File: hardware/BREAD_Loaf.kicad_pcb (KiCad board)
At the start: 2 copper layers, 35.4 x 50.7 mm, 33 parts, among them J2 THING_PLUS_LOGICAL, J6 PPPC101LGBN-RC, Q1 BSS138, Q2 BSS138, Q3 BSS138, U1 LTC4311ISC6-TRMPBF, U2 AP63205WU-7, U3 PCA9306

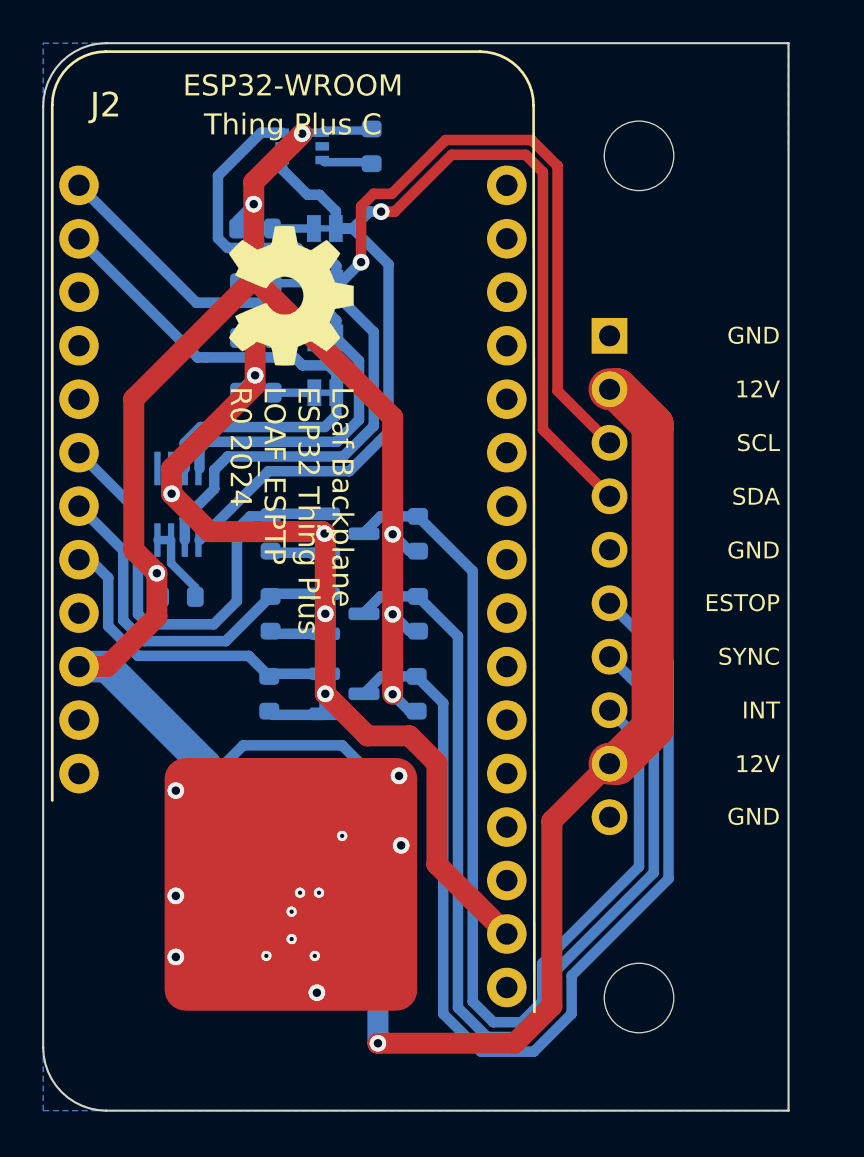
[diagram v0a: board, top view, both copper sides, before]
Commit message: added art and cleared erc errors
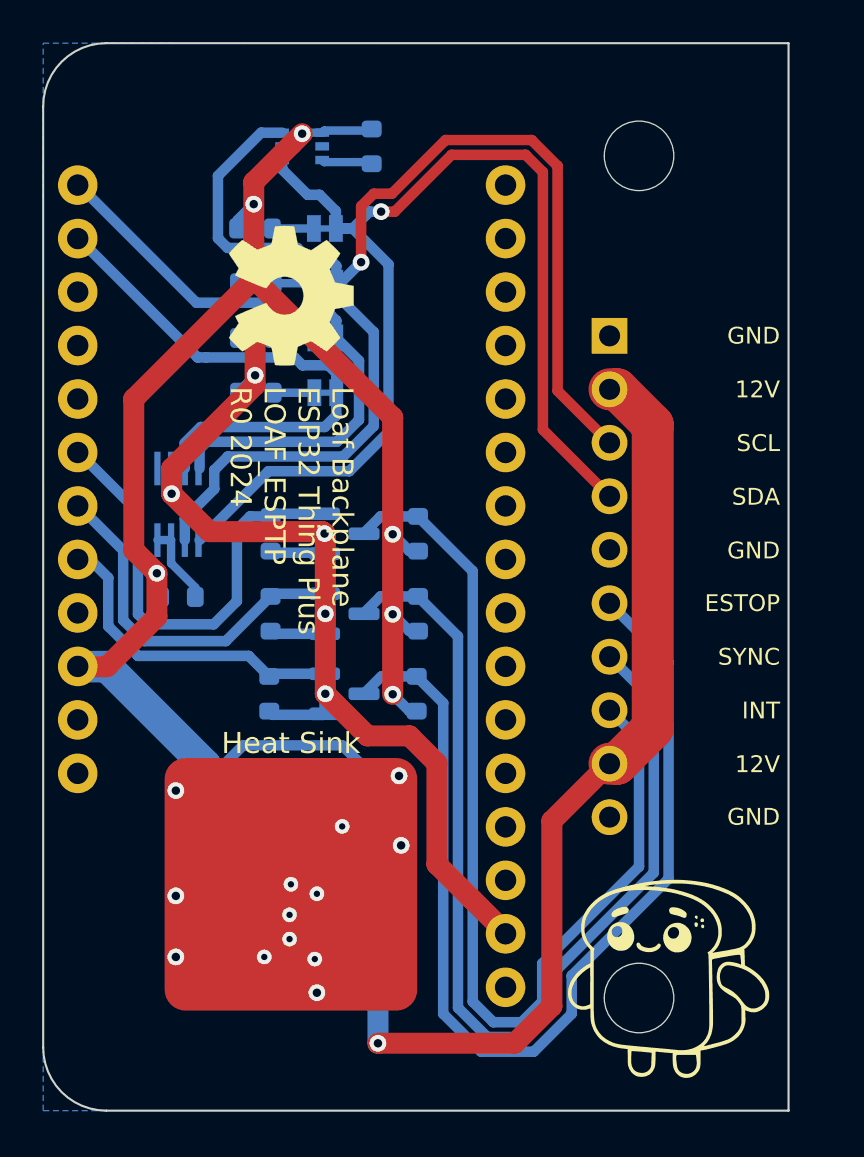
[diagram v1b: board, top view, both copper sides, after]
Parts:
- added demo**: Arc, Arc, F.Cu at (77.6, 122.4)
- added demo**: Arc, Arc, B.Cu at (86.4, 82.7)
- HS1: footprint SparkFun-Fuse:Thermal Pad -> KML-Custom:Thermal Pad
- J2: footprint SparkFun-RF:ESP_THING_PLUS -> SparkFun-Board:ThingPlus
- JP1, JP2, JP3, JP4: footprint SparkFun-Jumper:SMT-JUMPER_2_NC_TRACE_SILK -> SparkFun-Jumper:Jumper_2_NC_Trace
- ST1, ST2: footprint SparkFun-Hardware:STAND-OFF -> SparkFun-Hardware:Standoff
- moved J2 31.4 mm to (64.8, 102.6)

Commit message: updated to remove i2c shifter and optimized layout
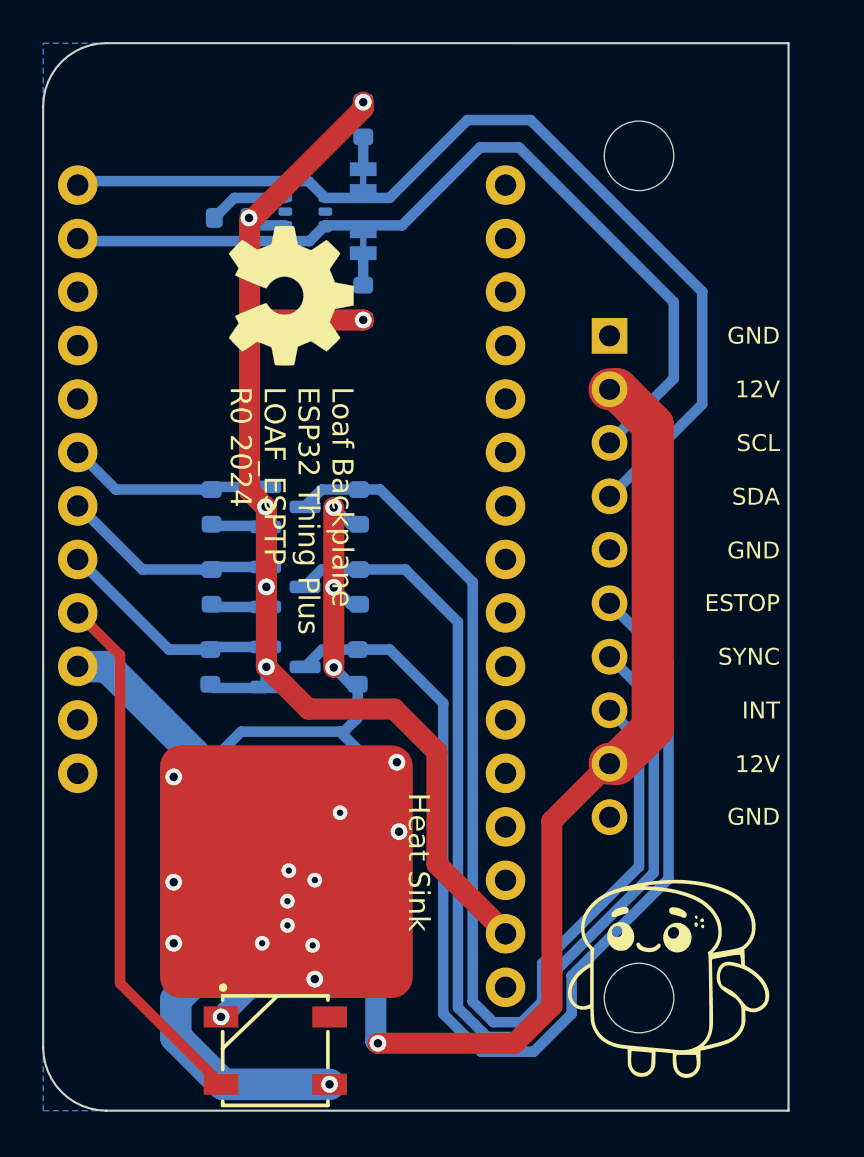
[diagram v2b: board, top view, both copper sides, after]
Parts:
- removed JP3, JP4: ~, SparkFun-Jumper:Jumper_2_NC_Trace
- removed R10, R12: 2.2k, Resistor_SMD:R_0603_1608Metric
- removed R11: 4.7k, Resistor_SMD:R_0603_1608Metric
- removed the U1 at (65.3, 77.9)
- removed U3: PCA9306, Package_SO:SSOP-8_2.95x2.8mm_P0.65mm
- removed the demo** at (86.4, 82.7)
- added D1: WS2812B_5050, SparkFun-LED:WS2812-5050-4PIN, F.Cu at (64.0, 120.8)
- added U2: LTC4311ISC6-TRMPBF, Package_TO_SOT_SMD:SOT-363_SC-70-6, B.Cu at (65.5, 81.0)
- R8: value 200k -> 2.2k
- R9: value 4.7k -> 2.2k
- moved R8 24.3 mm to (68.2, 76.6), turned to -90 degrees
- moved R7 7.47 mm to (62.0, 81.3), turned to 180 degrees
- moved R9 6.23 mm to (68.2, 85.3), turned to 90 degrees
- moved Q1 3.08 mm to (64.5, 102.6)
- moved R1 3.08 mm to (60.9, 102.6)
- moved R4 3.08 mm to (67.9, 102.6)
- moved Q2 3.08 mm to (64.5, 98.8)
- moved Q3 3.08 mm to (64.5, 95.0)
- moved R2 3.08 mm to (61.0, 98.8)
- moved R3 3.08 mm to (61.0, 95.0)
- moved R5 3.08 mm to (68.0, 98.8)
- moved R6 3.08 mm to (68.0, 95.0)
- moved JP1 2.93 mm to (68.2, 79.5), turned to -90 degrees
- moved JP2 2.65 mm to (68.2, 82.5), turned to 90 degrees
- moved C1 0.66 mm to (67.3, 114.3)
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- renumbered J6 to J1, U2 to U1
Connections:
- J1 pad 3: /SCL_5V -> /SCL_3.3V
- J1 pad 4: /SDA_5V -> /SDA_3.3V
- JP1 pad 2: /SDA_5V -> /SDA_3.3V
- JP2 pad 2: /SCL_5V -> /SCL_3.3V
- R7 pad 1: +5V -> +3.3V
- R8 pad 1: Net-(U3-EN) -> +3.3V
- R8 pad 2: +5V -> Net-(JP1-A)
- R9 pad 1: +5V -> +3.3V
- R9 pad 2: Net-(JP1-A) -> Net-(JP2-A)
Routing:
- net /SCL_5V: track 62.8 -> 0.00 mm, vias 1 -> 0
- net /SDA_5V: track 55.4 -> 0.00 mm, vias 1 -> 0
- net +5V: track 99.5 -> 60.0 mm, vias 7 -> 4
- net /LED_3.3V: track 0.00 -> 25.2 mm
- net /SDA_3.3V: track 29.1 -> 46.5 mm
- net /SCL_3.3V: track 26.0 -> 41.3 mm
- net /SYNC_3.3V: track 22.1 -> 9.64 mm
- net +3.3V: track 56.2 -> 67.4 mm
- net /INT_3.3V: track 17.2 -> 9.98 mm
- net /E_STOP_3.3V: track 15.4 -> 10.7 mm
- net Net-(U3-EN): track 3.83 -> 0.00 mm
- net /INT_5V: track 48.6 -> 52.2 mm
- net /E_STOP_5V: track 49.5 -> 52.9 mm
- net /SYNC_5V: track 47.5 -> 50.5 mm
- net GND: track 0.00 -> 2.89 mm, vias 13 -> 14
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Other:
- board text added: "I2C Accel. Pull-ups"
- board text removed: "I2C Extender"
- board text removed: "I2C Level Shifter"
- board text removed: "I2C Pullups"
- board text removed: "SCL 3.3V"
- board text removed: "SCL 5V"
- board text removed: "SDA 3.3V"
- board text removed: "SDA 5V"

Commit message: JLCPCB order rev-A
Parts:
- removed Logo1: Logo_Open_Hardware_Small, Symbol:OSHW-Symbol_6.7x6mm_SilkScreen
- added REF**: OSHW-Logo2_9.8x8mm_SilkScreen, Symbol:OSHW-Logo2_9.8x8mm_SilkScreen, B.Cu at (82.5, 78.3)
- moved demo** 38.8 mm to (77.7, 83.6)
- moved ST1 25.5 mm to (55.9, 76.0)
- moved ST2 5.28 mm to (85.9, 121.0)
- moved D1 0.20 mm to (64.0, 121.0)
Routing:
- net +5V: track 60.0 -> 56.6 mm
- net +12V: track 51.3 -> 50.6 mm
- net GND: track 2.89 -> 3.08 mm, vias 14 -> 13
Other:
- board size 35.4 x 50.7 mm -> 35.8 x 50.9 mm
- board text added: "BREAD Loaf ESP32 Controller (LOAF_ESPT) Cam K Brooks rev.A [09-2024]"
- board text removed: "Loaf Backplane ESP32 Thing Plus LOAF_ESPTP R0 2024"
